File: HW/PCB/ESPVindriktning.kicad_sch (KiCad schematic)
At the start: 104 parts, among them P101 TestPoint_Small, P102 TestPoint_Small, P103 TestPoint_Small, P104 TestPoint_Small, P105 TestPoint_Small, P106 TestPoint_Small, P107 TestPoint_Small, P108 TestPoint_Small, P109 TestPoint_Small, P110 TestPoint_Small, P111 TestPoint_Small, P112 TestPoint_Small, P113 TestPoint_Small, P114 TestPoint_Small, P115 TestPoint_Small, P116 TestPoint_Small, P117 TestPoint_Small, P118 TestPoint_Small, P119 TestPoint_Small, P120 TestPoint_Small, P121 TestPoint_Small, P122 TestPoint_Small, P123 TestPoint_Small, P124 TestPoint_Small, P125 TestPoint_Small, P126 TestPoint_Small, P127 TestPoint_Small, P128 TestPoint_Small, P129 TestPoint_Small, P130 TestPoint_Small, P131 TestPoint_Small, P132 TestPoint_Small, P133 TestPoint_Small, P134 TestPoint_Small, P135 TestPoint_Small, P136 TestPoint_Small, P137 TestPoint_Small, SW101 reset, SW102 boot, T101 BSS138, T102 BSS138, X101 USB_C, X102 WS2812, X105 Fan, X106 PM1006, X107 I2C, X108 UART

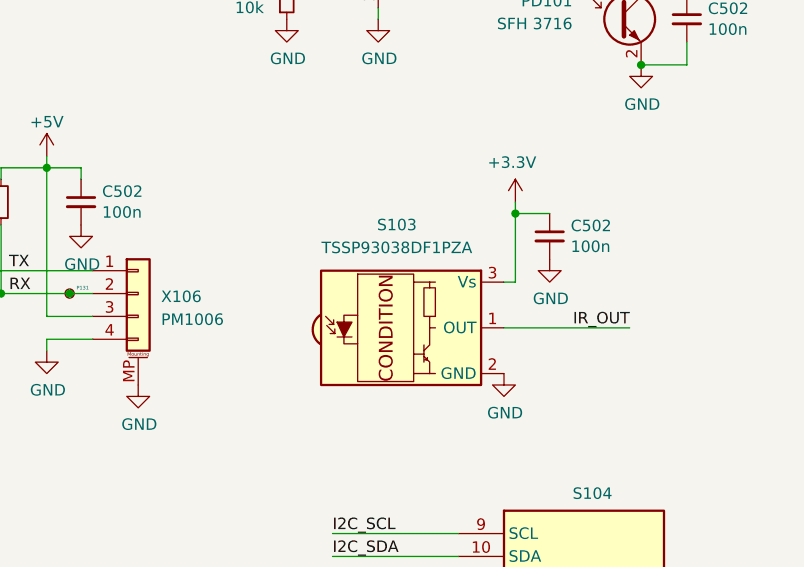
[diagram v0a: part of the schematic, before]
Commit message: Move ESP32 further into the PCB and replace IR receiver with smaller package
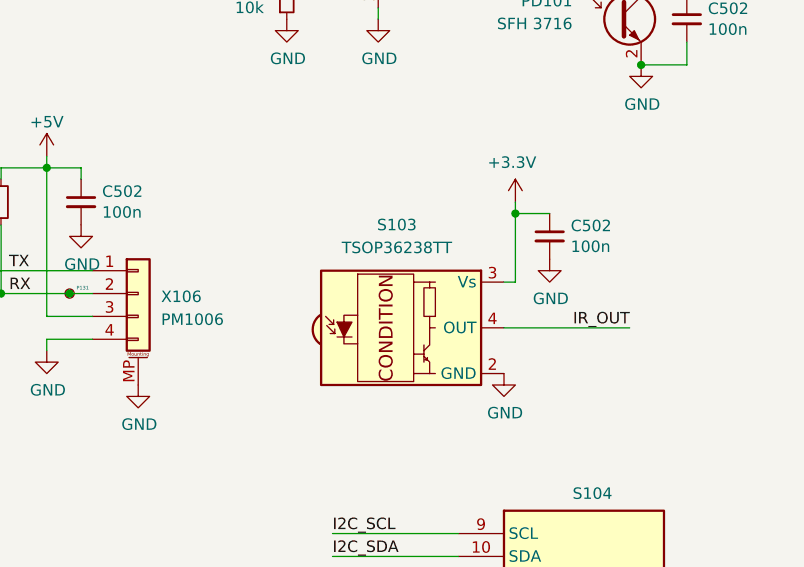
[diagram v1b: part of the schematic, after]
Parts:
- S103: value TSSP93038DF1PZA -> TSOP36238TT; footprint footprint:TSSP93038DF1PZA -> footprint:TSOP36238TT; Partnumber 78-TSSP93038DF1PZA -> 782-TSOP36238TT
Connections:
- net GND: now also S103.1 (GND)
- net IR_OUT: now also S103.4 (OUT); no longer S103.1 (OUT)
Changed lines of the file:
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@@
       (effects (font (size 1.27 1.27)))
     )
-    (property "Value" "TSSP93038DF1PZA" (at 239.565 74.93 0)
+    (property "Value" "TSOP36238TT" (at 239.565 74.93 0)
       (effects (font (size 1.27 1.27)))
     )
-    (property "Footprint" "footprint:TSSP93038DF1PZA" (at 240.03 93.345 0)
+    (property "Footprint" "footprint:TSOP36238TT" (at 240.03 93.345 0)
       (effects (font (size 1.27 1.27)) hide)
     )
@@
       (effects (font (size 1.27 1.27)) hide)
     )
-    (property "Partnumber" "78-TSSP93038DF1PZA" (at 241.3 83.82 0)
+    (property "Partnumber" "782-TSOP36238TT" (at 241.3 83.82 0)
       (effects (font (size 1.27 1.27)) hide)
     )
@@
     )
     (pin "3")
+    (pin "4")
+    (pin "2")
     (pin "1")
-    (pin "2")
     (instances
       (project "ESPVindriktning"

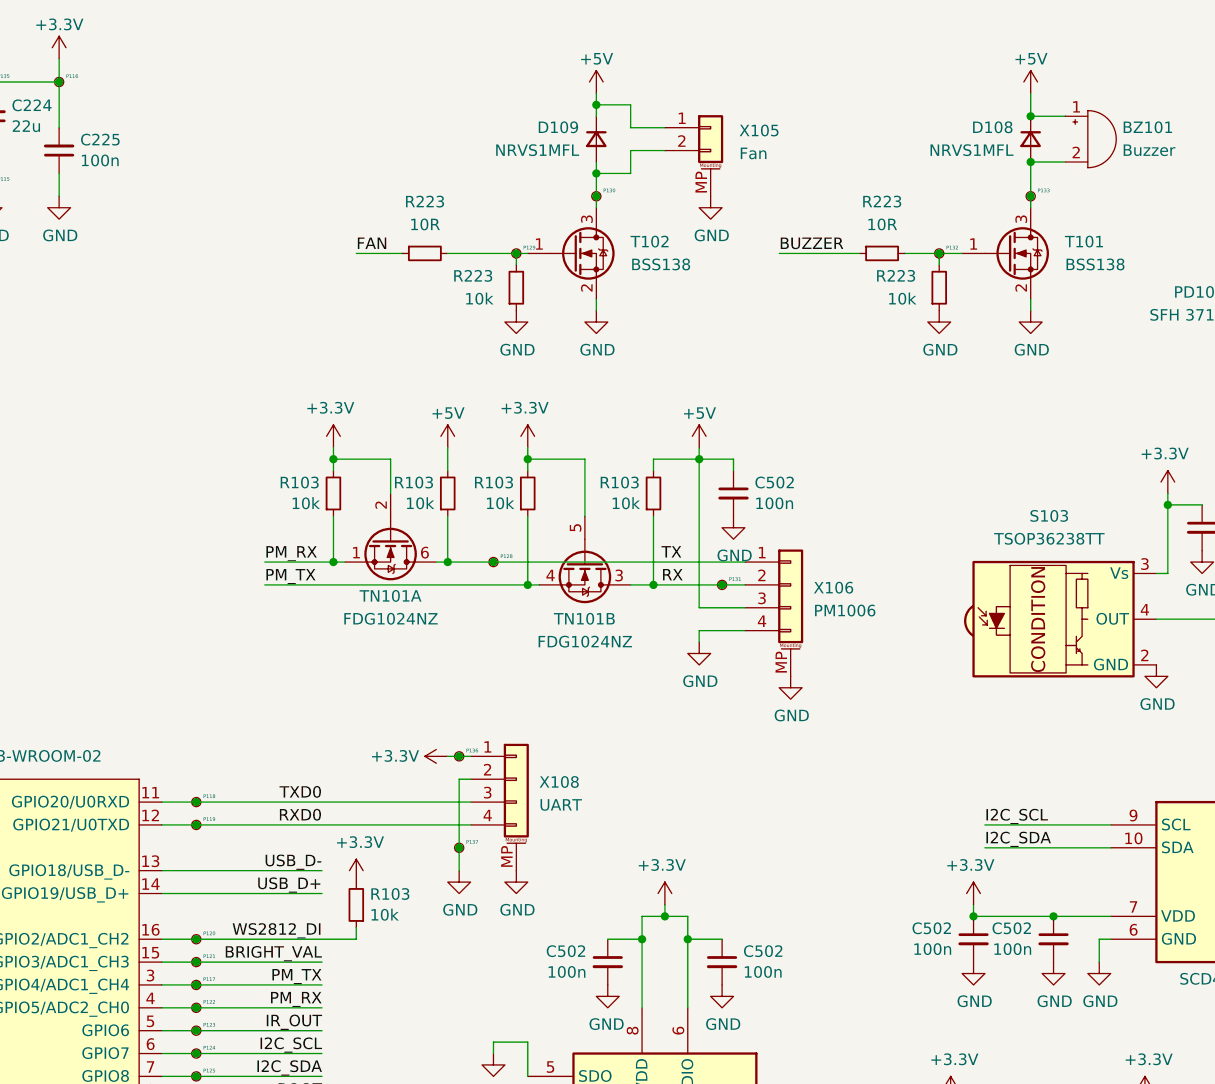
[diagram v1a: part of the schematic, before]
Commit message: Layout modifications to fit into housing
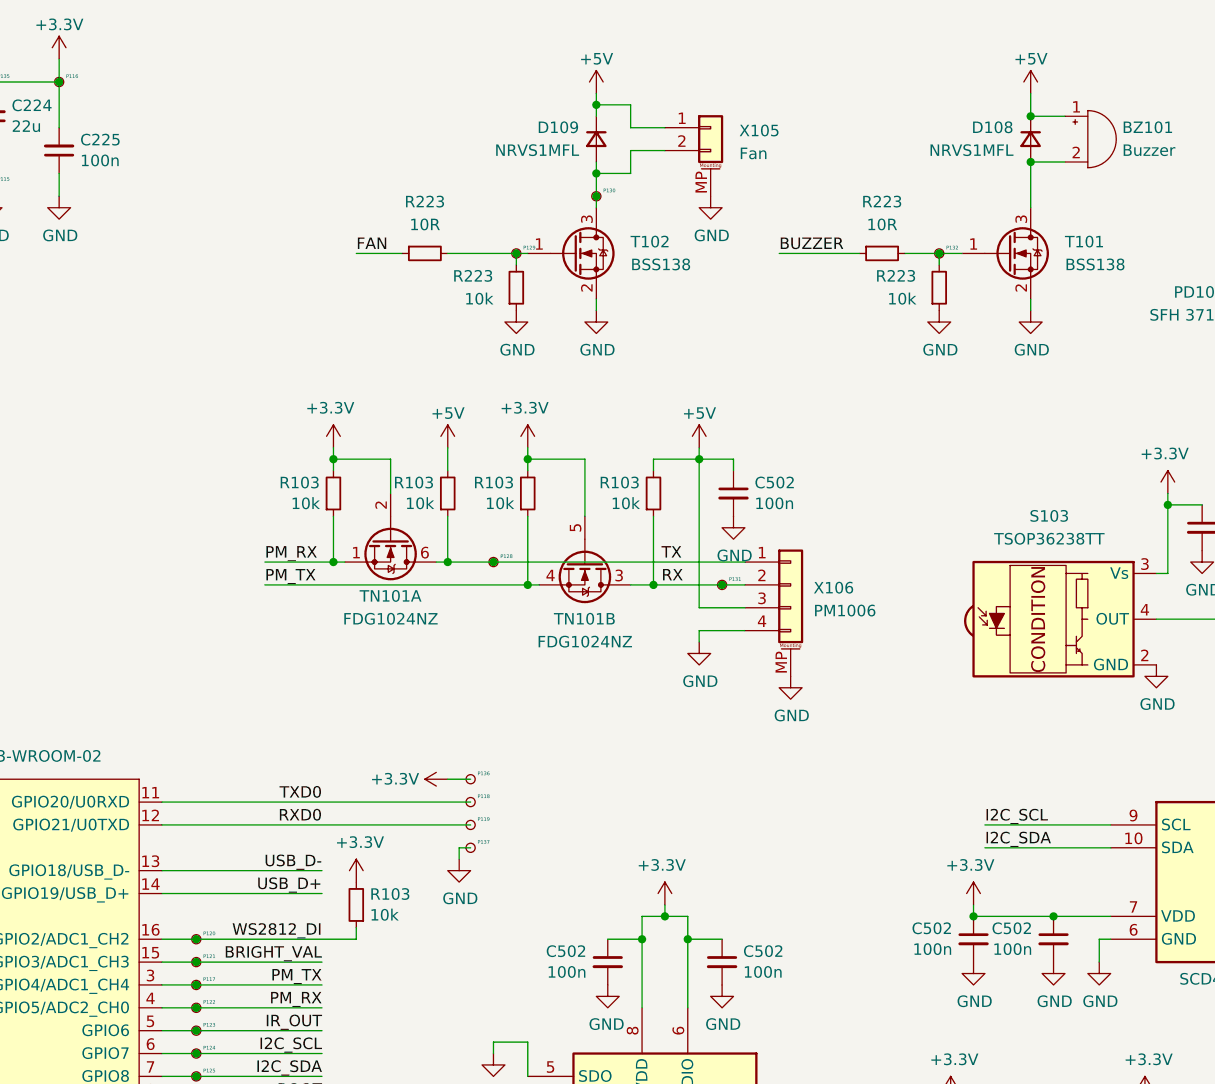
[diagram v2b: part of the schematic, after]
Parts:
- removed P133: TestPoint_Small, TestPoint:TestPoint_Pad_D1.0mm, symbol Connector:TestPoint_Small
- removed X108: UART, Connector_JST:JST_SH_BM04B-SRSS-TB_1x04-1MP_P1.00mm_Vertical, symbol Connector_Generic_MountingPin:Conn_01x04_MountingPin
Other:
- moved on the sheet: P118, P119, P136, P137

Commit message: Clean up schematic and layout further
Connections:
- net BUZ_G: now reaches P132.1, R223.2, R223.2, T101.1 (G)
- net CC1: now reaches P104.1, R102.2, X101.A5 (CC1)
- net CC2: now reaches P105.1, R101.2, X101.B5 (CC2)
- net ~{RST_BTN}: now reaches C102.1, D102.2 (A2), P101.1, R103.2, SW101.2
- net BOOT_BTN: now reaches C102.1, D104.2 (A2), P102.1, R103.2, SW102.2
- net STATUS_LED_R: now reaches D110.1 (K), R103.2
- net FAN_D: now reaches D109.2 (A), P130.1, T102.3 (D), X105.2 (Pin_2)
- net WS2812_3_DO: now reaches D107.2 (DOUT), P112.1, X102.3 (Pin_3)
- net FAN_G: now reaches P129.1, R223.2, R223.2, T102.1 (G)
- net BUZ_D: now reaches BZ101.2 (+), D108.2 (A), T101.3 (D)
- net WS2812_2_DO: now reaches D106.2 (DOUT), D107.4 (DIN), P107.1
- net WS2812_1_DO: now reaches D105.2 (DOUT), D106.4 (DIN), P103.1
- net STATUS_LED: now reaches D110.2 (A), P127.1, S102.10 (GPIO10)
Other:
- moved on the sheet: BZ101, C221, C222, C224, C225, C502, D108, P103, P104, P105, P107, P110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
